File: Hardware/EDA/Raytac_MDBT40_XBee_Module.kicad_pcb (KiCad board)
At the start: 2 copper layers, 24.4 x 24.5 mm, 29 parts, among them J1 HEADER_F_2.54MM_1R6P_ST_AU_PTH, J2 HEADER_F_2.54MM_1R6P_ST_AU_PTH, P1 XBee Pins Footprint, U1 MDBT40, Y1 32.768k

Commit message: Swapped CTS and RTS to correct for DTE perspective. Updated schematic.
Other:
- board text added: "Need to swap CTS/RTS"
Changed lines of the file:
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@@
     (links 66)
     (no_connects 0)
-    (area 98.809499 80.309499 123.590501 105.190501)
+    (area 98.458172 80.309499 125.541829 110.7748)
     (thickness 1.6002)
-    (drawings 10)
+    (drawings 11)
     (tracks 323)
     (zones 0)
@@
       (net 55 /RTS) (solder_mask_margin 0.254))
   )
+  (gr_text "Need to swap CTS/RTS" (at 112 109.2) (layer Cmts.User)
+    (effects (font (size 2.032 1.524) (thickness 0.3048)))
+  )
   (gr_text Link (at 118.9 102.8) (layer F.SilkS)

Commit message: Changed board outline to conform to standard Digi XBee outline.
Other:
- board text added: "Change board outline to conform to standard Digi XBee outline."
- board text removed: "Need to swap CTS/RTS"
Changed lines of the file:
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@@
     (links 66)
     (no_connects 0)
-    (area 98.458172 80.309499 125.541829 110.7748)
+    (area 98.809499 80.309499 140.139257 114.1496)
     (thickness 1.6002)
     (drawings 11)
@@
       (net 55 /RTS) (solder_mask_margin 0.254))
   )
-  (gr_text "Need to swap CTS/RTS" (at 112 109.2) (layer Cmts.User)
-    (effects (font (size 2.032 1.524) (thickness 0.3048)))
+  (gr_text "Change board outline to conform \nto standard Digi XBee outline. " (at 100 111) (layer Cmts.User)
+    (effects (font (size 2.032 1.524) (thickness 0.3048)) (justify left))
   )
   (gr_text Link (at 118.9 102.8) (layer F.SilkS)

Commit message: Updated to remove BLE Nano headers.  PCB layout incomplete!
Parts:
- removed J1, J2: HEADER_F_2.54MM_1R6P_ST_AU_PTH, Header:HEADER_F_2.54MM_1R6P_ST_AU_PTH
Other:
- board size 24.4 x 24.5 mm -> 24.4 x 27.6 mm
- board text removed: "Change board outline to conform to standard Digi XBee outline."

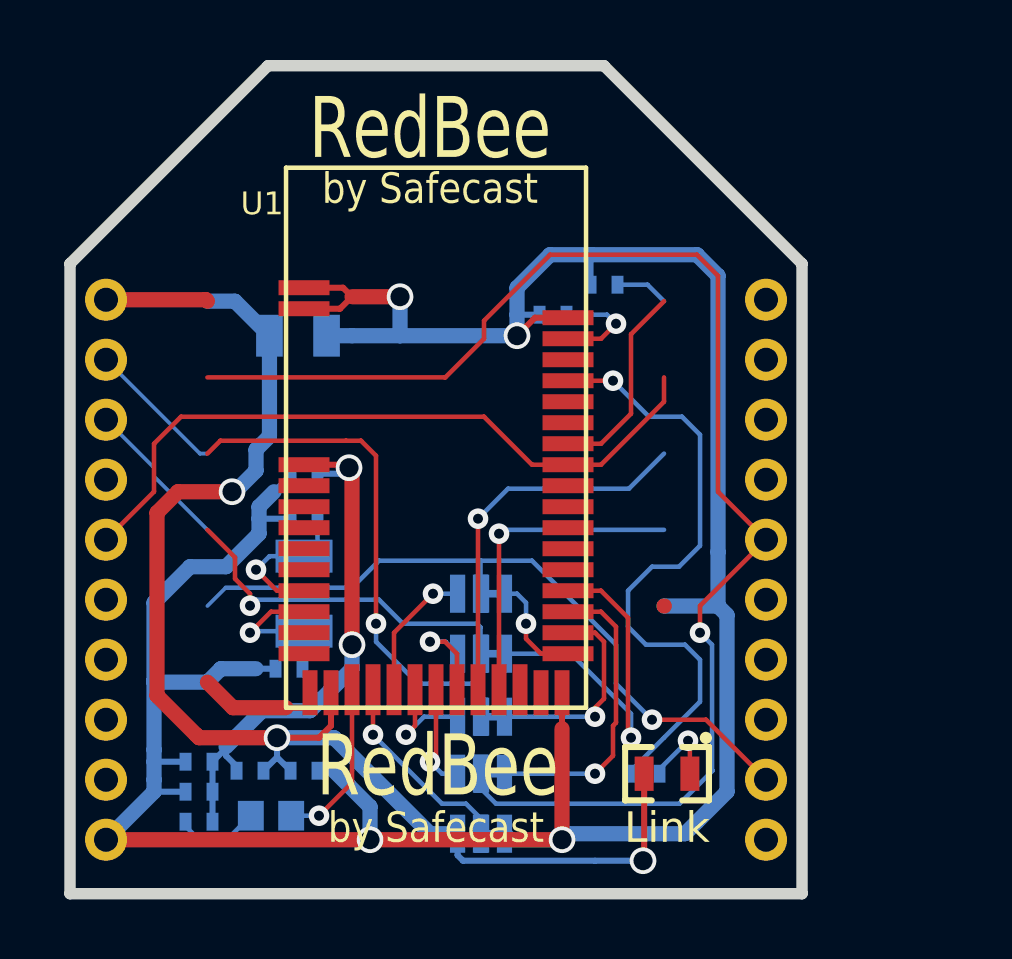
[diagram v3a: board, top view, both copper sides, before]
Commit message: Updated schematic and board layout.  About halfway done routing.
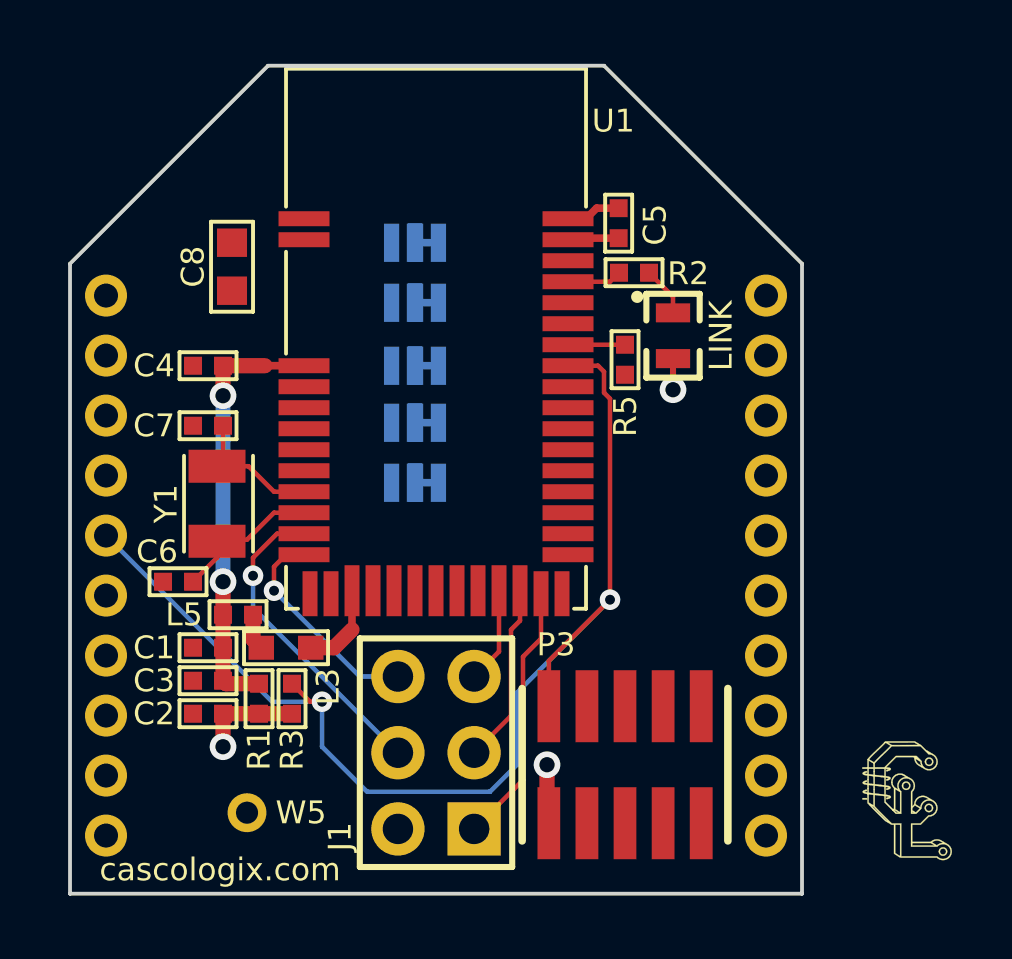
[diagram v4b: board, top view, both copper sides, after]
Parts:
- added G***: LOGO, Logo:Casco_Logix_Logo_4x4MM, F.Cu at (126.9, 101.9)
- added J1: TEST POINTS, Header:HEADER_F_100MIL_2R6P_ST_GOLD_PTH, F.Cu at (111.2, 100.3)
- added P2: HEADER_M_XBEE_P11-P20_PTH_DTE, Header:HEADER_XBEE_P11_P20_ALT3, B.Cu at (122.2, 93.1)
- added P3: JTAG, Header:HEADER_M_1.27MM_2R10P_ST_AU_SMT, F.Cu at (117.5, 100.7)
- added R3: 12k, Passive:R0402, F.Cu at (106.4, 98.5)
- added W5: WIRE_PAD_24AWG, Wire_to_Board:WIRE_PAD_24AWG, F.Cu at (104.9, 102.3)
- C1, C2, C3, C4, C5, C6, C7: footprint Passive:0402 -> Passive:C0402; moved to F.Cu
- C8: footprint Passive:0805 -> Passive:C0603; moved to F.Cu
- L3: footprint Passive:0603 -> Passive:L0603; moved to F.Cu
- L5: footprint Passive:0402 -> Passive:L0402; moved to F.Cu
- P1: value XBee Pins Footprint -> XBEE MODULE PINS; footprint Header:HEADER_XBEE -> Header:HEADER_XBEE_P1_P10_ALT3
- R1, R2, R5: footprint Passive:0402 -> Passive:R0402; moved to F.Cu
- U1: footprint RF_Modules:MDBT40 -> MDBT40
- Y1: moved to F.Cu
- moved R2 16.7 mm to (117.8, 84.3)
- moved DS1 14.6 mm to (119.1, 86.4), turned to 270 degrees
- moved S10 11.9 mm to (110.1, 91.3)
- moved S6 11.9 mm to (110.1, 83.3)
- moved S7 11.9 mm to (110.1, 85.3)
- moved S9 11.9 mm to (110.1, 89.3)
- moved S1 11.9 mm to (110.9, 83.3)
- moved S2 11.9 mm to (110.9, 85.3)
- moved S4 11.9 mm to (110.9, 89.3)
- moved S5 11.9 mm to (110.9, 91.3)
- moved S8 11.9 mm to (110.1, 87.4)
- moved S3 11.9 mm to (110.9, 87.4)
- moved P1 7.86 mm to (111.2, 93.1)
- moved L5 7.02 mm to (104.6, 95.7)
- moved L3 5.62 mm to (106.2, 96.8), turned to 0 degrees
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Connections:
- net RESET renamed SWDIO/RESET
- C1 pad 1: VAA -> VDDA
- C3 pad 1: VAA -> VDDA
- C4 pad 2: VAA -> VDDA
- L5 pad 1: Net-(L3-Pad2) -> VDDA
- L5 pad 2: VAA -> Net-(L3-Pad1)
- R1 pad 2: VAA -> VDDA
- U1 pad 11: Net-(U1-Pad11) -> P0.28
- U1 pad 12: Net-(U1-Pad12) -> P0.29
- U1 pad 15: Net-(L3-Pad1) -> Net-(L3-Pad2)
- U1 pad 23: Net-(U1-Pad23) -> P0.06
- U1 pad 24: Net-(U1-Pad24) -> P0.07
- U1 pad 3: VAA -> VDDA
- U1 pad 33: Net-(U1-Pad33) -> P0.15
- Y1 pad 1: Net-(C6-Pad1) -> Net-(C7-Pad1)
- Y1 pad 2: Net-(C7-Pad1) -> Net-(C6-Pad1)
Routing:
- net GND: track 104.4 -> 1.23 mm, vias 4 -> 0
- net CTS_HEADER: track 46.5 -> 0.00 mm, vias 1 -> 0
- net VDD: track 46.9 -> 6.41 mm
- net RTS_HEADER: track 24.1 -> 0.00 mm, vias 1 -> 0
- net TXD_HEADER: track 22.0 -> 0.00 mm, vias 1 -> 0
- net VAA: track 18.9 -> 0.00 mm, vias 2 -> 0
- net Net-(R2-Pad1): track 20.1 -> 1.22 mm, vias 1 -> 0
- net RXD_HEADER: track 17.2 -> 0.00 mm, vias 1 -> 0
- net SWDIO/RESET: track 23.6 -> 39.6 mm, vias 0 -> 2
- net VDDA: track 0.00 -> 13.9 mm, vias 0 -> 2
- net P0.04: track 13.4 -> 0.00 mm, vias 1 -> 0
- net /RXD: track 11.7 -> 0.00 mm, vias 1 -> 0
- net P0.28: track 0.00 -> 9.93 mm, vias 0 -> 1
- net /CTS: track 9.42 -> 0.00 mm, vias 1 -> 0
- net P0.05: track 11.4 -> 2.60 mm, vias 1 -> 0
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- added copper zone on F.Cu, net GND
- added copper zone on B.Cu, net VDD
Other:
- net class Power: via_drill 0.635 -> 0.508
- board text added: "LINK"
- board text added: "MDBT40 XBee"
- board text added: "REV 0.1"
- board text added: "cascologix.com"
- board text removed: "Link"
- board text removed: "RedBee"
- board text removed: "Rev 1.0.0"
- board text removed: "by Safecast"

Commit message: Moved solder links to make routing easier.
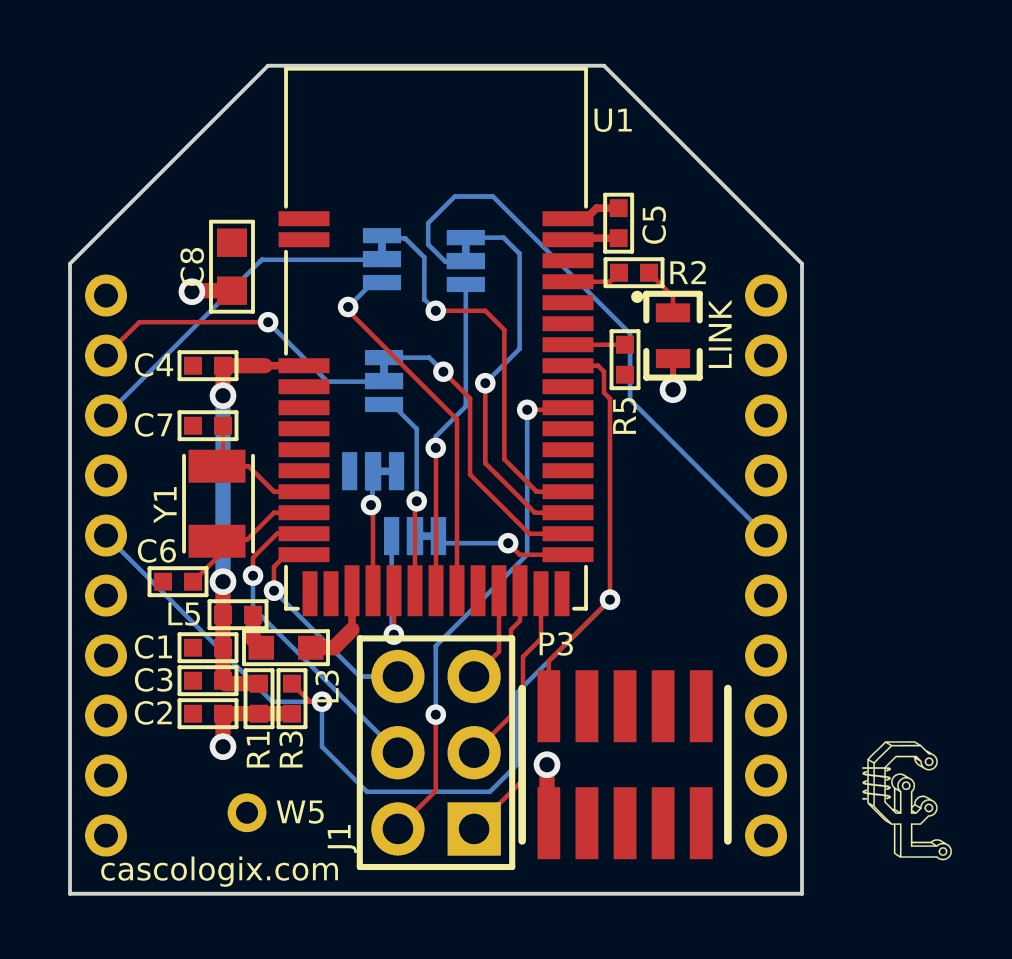
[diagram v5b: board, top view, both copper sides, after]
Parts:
- moved S1 9.78 mm to (110.9, 93.1)
- moved S6 9.78 mm to (110.1, 93.1)
- moved S4 5.93 mm to (112.2, 83.5), turned to 90 degrees
- moved S9 5.41 mm to (112.2, 84.3), turned to 270 degrees
- moved S2 2.38 mm to (109.4, 83.4), turned to 90 degrees
- moved S5 1.45 mm to (109.5, 90.9)
- moved S10 1.45 mm to (108.7, 90.9)
- moved S3 1.44 mm to (109.5, 87.5), turned to 90 degrees
- moved S7 1.26 mm to (109.4, 84.2), turned to 270 degrees
- moved S8 1.11 mm to (109.5, 88.3), turned to 270 degrees
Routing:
- net CTS_HEADER: track 0.00 -> 20.4 mm
- net P0.15: track 0.00 -> 17.7 mm, vias 0 -> 2
- net /RXD: track 0.00 -> 13.7 mm, vias 0 -> 1
- net /CTS: track 0.00 -> 13.5 mm, vias 0 -> 1
- net Net-(S7-Pad2): track 0.00 -> 13.0 mm, vias 0 -> 1
- net RXD_HEADER: track 0.00 -> 11.4 mm
- net Net-(S9-Pad2): track 0.00 -> 11.2 mm, vias 0 -> 1
- net /TXD: track 0.00 -> 10.7 mm, vias 0 -> 1
- net TXD_HEADER: track 0.00 -> 10.5 mm, vias 0 -> 1
- net Net-(S8-Pad2): track 0.00 -> 7.59 mm, vias 0 -> 1
- net /RTS: track 0.00 -> 5.18 mm, vias 0 -> 1
- net Net-(S10-Pad2): track 0.00 -> 4.63 mm, vias 0 -> 1
- net Net-(S6-Pad2): track 0.00 -> 4.18 mm, vias 0 -> 1
- net VDD: track 6.41 -> 7.76 mm, vias 3 -> 4
